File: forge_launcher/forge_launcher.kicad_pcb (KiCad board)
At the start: 4 copper layers, 151.1 x 106 mm, 201 parts, among them J10 Screw_Terminal_01x02, J11 Screw_Terminal_01x02, J12 Screw_Terminal_01x02, J3 Conn_01x06, J7 Screw_Terminal_01x02, J9 Screw_Terminal_01x02, Q1 STR2P3LLH6(Pfet), Q10 MMBT3904, Q2 2N3904, Q3 MMBT3904, Q4 IPD60R145, Q6 IPD60R145, Q9 MMBT3904, SW10 LAUNCH, SW3 ARM, U1 LT3420, U10 AMC3330, U14 AMC3302, U17 AD7352, U18 IR2127, U2 TLV74318, U23 TLV74325, U3 AD7352, U4 TLV74325, U5 LMO78_03-1.0, U6 4945, U8 AMC3330

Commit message: handheld controller PCB layout. Caps, Coil and 4xAA battery holder on bottom side. 2 buttons, 2 leds on topside. ForgeFPGA can mount below with battery removed and 02x13 header sockets added. Will 3d print minimum volume case with buttons and lite pipes.
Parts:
- removed the BT1 at (116.3, 80.8)
- removed the BT1 at (157.5, 80.6)
- removed the H13 at (90.2, 95.2)
- removed the H15 at (91.4, 109.2)
- removed J12: Screw_Terminal_01x02, TerminalBlock_Phoenix:TerminalBlock_Phoenix_MKDS-1,5-2-5.08_1x02_P5.08mm_Horizontal
- removed the PS1 at (236.1, 97.7)
- removed REF** (x2): PinSocket_2x13_P2.54mm_Vertical, Connector_PinSocket_2.54mm:PinSocket_2x13_P2.54mm_Vertical
- removed REF**: SC-82AA, Package_TO_SOT_SMD:SC-82AA
- removed the U5 at (247.1, 96.9)
- removed the U6 at (241.6, 96.9)
- added BT1: ~, myspace pcb:BAT_BH4AA-PC, B.Cu at (233.9, 115.1)
- added C24: 100u 400V, myspace pcb:CAP_radial_18mmdia_38mmh, B.Cu at (213.2, 33.8)
- added C25: 100u 400V, myspace pcb:CAP_radial_18mmdia_38mmh_L, B.Cu at (261.5, 33.8)
- added L1: 390uH 5A, Inductor_THT:L_Toroid_Horizontal_D32.5mm_P28.90mm_Bourns_2300, B.Cu at (234.9, 70.8)
- C17: value CP_Radial_Tantal_D8.0mm_P2.50mm -> 100u 20v
- C18, D1, Q10, Q3, Q9, R108, R11, R15, R31, R32, R4, U2, U23, U4: moved to F.Cu
- J1, J2: renamed from REF**; value PinSocket_2x13_P2.54mm_Vertical -> Conn_02x13_Odd_Even
- J7: moved to B.Cu
- U5: renamed from REF**; value Converter_DCDC_Murata_OKI-78SR_Horizontal -> LMO78_03-1.0
- U6: renamed from REF**; value Converter_DCDC_Murata_OKI-78SR_Horizontal -> 4945
- moved H4 202.9 mm to (264.8, 109.9)
- moved H11 195.1 mm to (234.3, 142.2)
- moved H8 193.5 mm to (245.7, 106.7)
- moved H10 187.8 mm to (259.7, 45.1)
- moved H14 160.2 mm to (264.8, 29.8)
- moved C15 155.6 mm to (259.1, 74.9)
- moved U1 153.9 mm to (264.2, 91.4), turned to 0 degrees
- moved TR1 150.0 mm to (260.4, 82.5), turned to 45 degrees
- moved D5 149.0 mm to (259.4, 71.5), turned to 90 degrees
- moved Q6 146.5 mm to (245.7, 67.3), turned to 90 degrees
- moved R3 143.8 mm to (244.5, 49.5), turned to 90 degrees
- moved C16 142.6 mm to (258.4, 92.1), turned to 90 degrees
- moved C19 140.2 mm to (255.3, 91.4), turned to 90 degrees
- moved H12 136.5 mm to (207.0, 44.5)
- moved H13 133.4 mm to (224.2, 106.0)
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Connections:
- C17 pad 1: (no net) -> Net-(D3-A)
- C17 pad 2: (no net) -> GND
- J1 pad 1: (no net) -> unconnected-(J1-Pin_1-Pad1)
- J1 pad 10: (no net) -> GND
- J1 pad 11: (no net) -> unconnected-(J1-Pin_11-Pad11)
- J1 pad 12: (no net) -> GND
- J1 pad 13: (no net) -> unconnected-(J1-Pin_13-Pad13)
- J1 pad 14: (no net) -> GND
- J1 pad 15: (no net) -> unconnected-(J1-Pin_15-Pad15)
- J1 pad 16: (no net) -> GND
- J1 pad 17: (no net) -> unconnected-(J1-Pin_17-Pad17)
- J1 pad 18: (no net) -> GND
- J1 pad 19: (no net) -> unconnected-(J1-Pin_19-Pad19)
- J1 pad 2: (no net) -> GND
- J1 pad 20: (no net) -> GND
- J1 pad 21: (no net) -> unconnected-(J1-Pin_21-Pad21)
- J1 pad 22: (no net) -> GND
- J1 pad 23: (no net) -> unconnected-(J1-Pin_23-Pad23)
- J1 pad 24: (no net) -> GND
- J1 pad 25: (no net) -> unconnected-(J1-Pin_25-Pad25)
- J1 pad 26: (no net) -> GND
- J1 pad 3: (no net) -> unconnected-(J1-Pin_3-Pad3)
- J1 pad 4: (no net) -> GND
- J1 pad 5: (no net) -> unconnected-(J1-Pin_5-Pad5)
- J1 pad 6: (no net) -> GND
- J1 pad 7: (no net) -> unconnected-(J1-Pin_7-Pad7)
- J1 pad 8: (no net) -> GND
- J1 pad 9: (no net) -> unconnected-(J1-Pin_9-Pad9)
- J2 pad 1: (no net) -> GND
- J2 pad 10: (no net) -> unconnected-(J2-Pin_10-Pad10)
- J2 pad 11: (no net) -> GND
- J2 pad 12: (no net) -> unconnected-(J2-Pin_12-Pad12)
- J2 pad 13: (no net) -> GND
- J2 pad 14: (no net) -> unconnected-(J2-Pin_14-Pad14)
- J2 pad 15: (no net) -> GND
- J2 pad 16: (no net) -> unconnected-(J2-Pin_16-Pad16)
- J2 pad 17: (no net) -> GND
- J2 pad 18: (no net) -> unconnected-(J2-Pin_18-Pad18)
- J2 pad 19: (no net) -> GND
- J2 pad 2: (no net) -> unconnected-(J2-Pin_2-Pad2)
- J2 pad 20: (no net) -> unconnected-(J2-Pin_20-Pad20)
- J2 pad 21: (no net) -> GND
- J2 pad 22: (no net) -> unconnected-(J2-Pin_22-Pad22)
- J2 pad 23: (no net) -> GND
- J2 pad 24: (no net) -> unconnected-(J2-Pin_24-Pad24)
- J2 pad 25: (no net) -> GND
- J2 pad 26: (no net) -> unconnected-(J2-Pin_26-Pad26)
- J2 pad 3: (no net) -> GND
- J2 pad 4: (no net) -> unconnected-(J2-Pin_4-Pad4)
- J2 pad 5: (no net) -> GND
- J2 pad 6: (no net) -> unconnected-(J2-Pin_6-Pad6)
- J2 pad 7: (no net) -> GND
- J2 pad 8: (no net) -> unconnected-(J2-Pin_8-Pad8)
- J2 pad 9: (no net) -> GND
- U19 pad 25: (no net) -> GND
- U5 pad 1: (no net) -> +12V
- U5 pad 2: (no net) -> GND
- U5 pad 3: (no net) -> +3.3V
- U6 pad 1: (no net) -> +BATT
- U6 pad 2: (no net) -> GND
- U6 pad 3: (no net) -> +12V
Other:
- board size 151.1 x 106 mm -> 68 x 118 mm
- board text added: "CASE"
- board text added: "CHARGE"
- board text added: "CONT"
- board text removed: "B"

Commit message: Landscape style PCB initial layout 3d. Large components on bottom as per model. Forge emulator connector section of PCB can be cut away, but also has a spare fpga land point.
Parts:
- removed J10, J11, J7: Screw_Terminal_01x02, TerminalBlock_Phoenix:TerminalBlock_Phoenix_MKDS-1,5-2-5.08_1x02_P5.08mm_Horizontal
- added BT2: BatteryHolder_Keystone_2462_2xAA, Battery:BatteryHolder_Keystone_2462_2xAA, B.Cu at (115.5, 104.2)
- added D6: ES1J, Diode_SMD:D_SMA, F.Cu at (168.3, 64.1)
- added D7: ES1J, Diode_SMD:D_SMA, F.Cu at (168.3, 67.9)
- added R12: 10K, Resistor_SMD:R_0603_1608Metric, B.Cu at (184.2, 78.1)
- added REF**: CalTest_CT3151, Connector:CalTest_CT3151, B.Cu at (153.5, 42.3)
- added REF**: CalTest_CT3151, Connector:CalTest_CT3151, B.Cu at (131.0, 42.3)
- added U19: ~, Package_DFN_QFN:QFN-24-1EP_3x3mm_P0.4mm_EP1.75x1.6mm_ThermalVias, F.Cu at (144.5, 131.5)
- added U2: TLV74318, Package_TO_SOT_SMD:SOT-23-5, B.Cu at (134.5, 132.0)
- BT1: footprint myspace pcb:BAT_BH4AA-PC -> Battery:BatteryHolder_Keystone_2462_2xAA
- C16, C18, C19, D1, D3, PS1, Q1, Q10, Q2, Q3, Q9, R1, R10, R108, R11, R110, R13, R15, R2, R29, R31, R32, R4, R5, R8, U2, U23, U4: moved to B.Cu
- C17: footprint Capacitor_THT:CP_Radial_Tantal_D8.0mm_P2.50mm -> Capacitor_THT:CP_Radial_D8.0mm_P5.00mm; moved to B.Cu
- J9: footprint TerminalBlock_Phoenix:TerminalBlock_Phoenix_MKDS-1,5-2-5.08_1x02_P5.08mm_Horizontal -> Connector_BarrelJack:BarrelJack_CUI_PJ-102AH_Horizontal
- L1: footprint Inductor_THT:L_Toroid_Horizontal_D32.5mm_P28.90mm_Bourns_2300 -> Inductor_THT:L_Toroid_Vertical_L31.8mm_W15.9mm_P13.50mm_Bourns_5700
- moved H4 184.0 mm to (93.3, 43.2)
- moved H12 155.3 mm to (93.5, 150.5)
- moved H5 136.8 mm to (93.5, 111.5)
- moved TP1 135.7 mm to (20.9, 99.4)
- moved TP2 135.7 mm to (20.9, 103.7)
- moved TP3 135.7 mm to (25.2, 99.4)
- moved TP4 135.7 mm to (25.2, 103.7)
- moved TP5 135.7 mm to (29.6, 99.4)
- moved TP6 135.7 mm to (29.6, 103.7)
- moved H11 133.5 mm to (144.8, 43.2)
- moved J9 129.9 mm to (104.8, 84.5), turned to -90 degrees
- moved R20 126.2 mm to (36.7, 88.4)
- moved R21 126.2 mm to (36.7, 90.9)
- moved R22 126.2 mm to (36.7, 93.5)
- moved R24 126.2 mm to (36.7, 96.0)
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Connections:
- C14 pad 1: +1V8 -> +1V1
- C17 pad 1: Net-(D3-A) -> Net-(D6-K)
- Q1 pad 1: Net-(Q1-G) -> Net-(D7-K)
- Q1 pad 2: Net-(D3-A) -> Net-(D6-K)
- Q2 pad 3: Net-(Q1-G) -> Net-(D7-A)
- R1 pad 2: Net-(Q1-G) -> Net-(D7-K)
- U19 pad 22: +1V2 -> +1V1
- U2 pad 5: +1V8 -> +1V1
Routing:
- net GND: track 19.9 -> 0.00 mm, vias 1 -> 0
- net /DisG: track 1.19 -> 0.00 mm
- net (no net): vias 0 -> 48
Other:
- board size 68 x 118 mm -> 109 x 115 mm
- board text added: "ForgeFPGA Eval Board Connector"
- board text added: "spare"
- board text removed: "1"
- board text removed: "2"
- board text removed: "CASE"

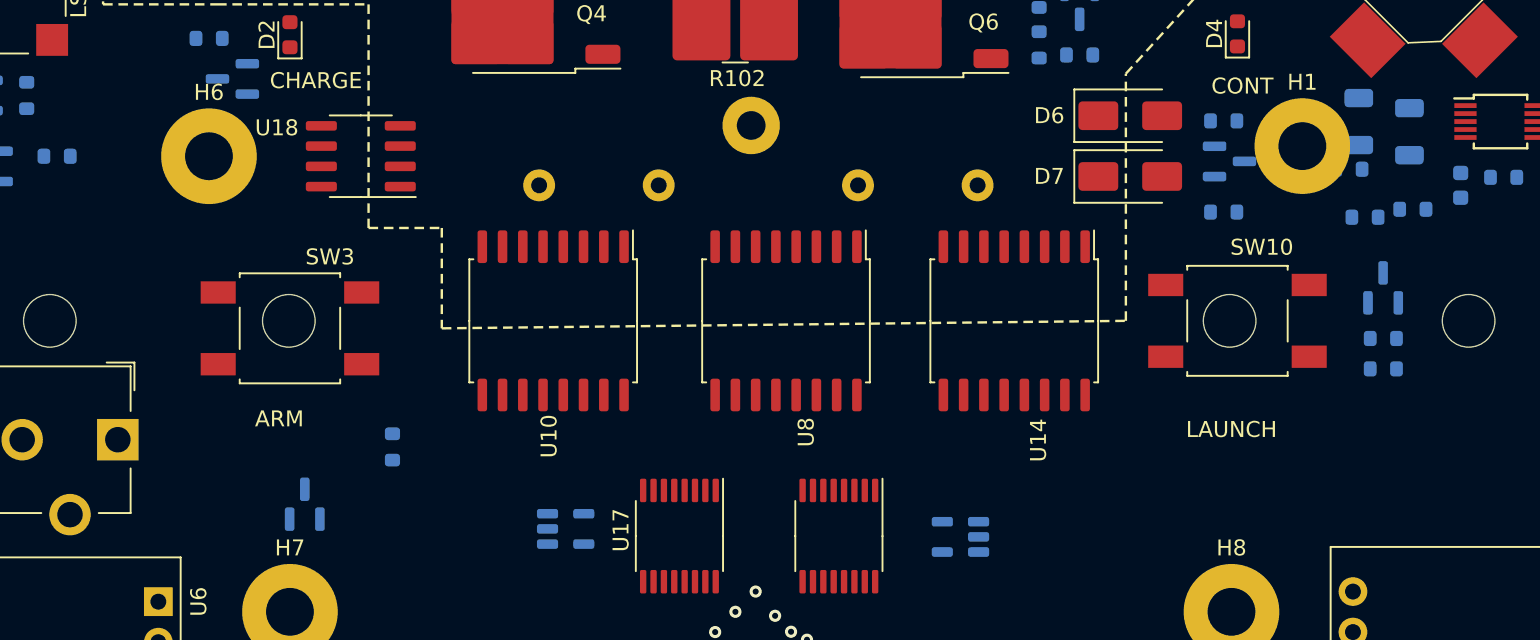
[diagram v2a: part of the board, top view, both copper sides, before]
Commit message: Added component for 3d button frogs (better name than push-button-with-spring-for-tactile-switch)
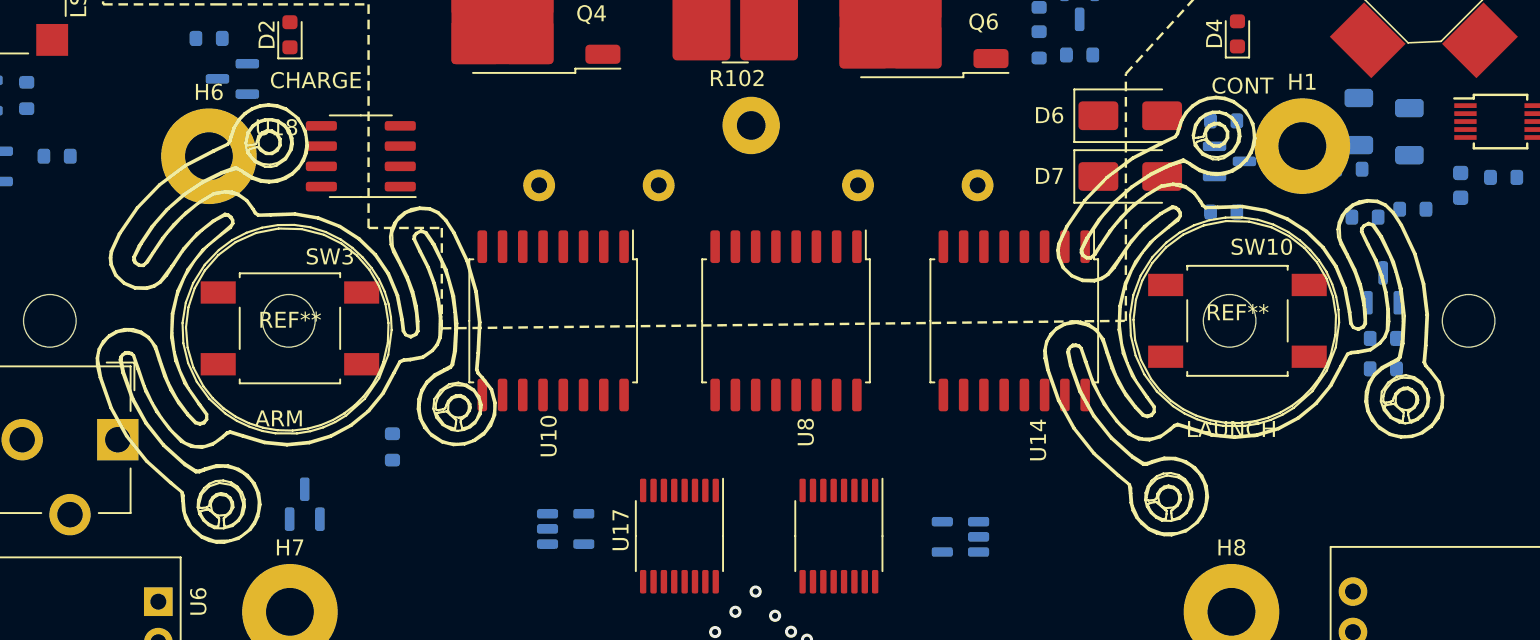
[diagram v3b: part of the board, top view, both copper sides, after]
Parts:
- added REF**: button_frog, myspace pcb:button_frog, F.Cu at (115.6, 77.5)
- added REF**: button_frog, myspace pcb:button_frog, F.Cu at (175.0, 77.0)

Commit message: Update to last ver before fork
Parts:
- removed D3: BAV99, Package_TO_SOT_SMD:SOT-23
- removed FB2: Ferrite, Inductor_SMD:L_0603_1608Metric
- removed the H1 at (179.1, 66.0)
- removed H10, H11, H12, H14, H15, H5, H6, H7, H8: ~, MountingHole:MountingHole_3mm_Pad
- removed J3: Conn_01x06, Connector_PinHeader_2.54mm:PinHeader_1x06_P2.54mm_Vertical
- removed R86: 22R, Resistor_SMD:R_0603_1608Metric
- added C27: 0.1u, Capacitor_SMD:C_0603_1608Metric, B.Cu at (180.1, 65.3)
- added C28: 1u, Capacitor_SMD:C_0603_1608Metric, B.Cu at (161.8, 99.6)
- added C29: 2.2n, Capacitor_SMD:C_0603_1608Metric, B.Cu at (148.6, 86.9)
- added C30: 2.2n, Capacitor_SMD:C_0603_1608Metric, B.Cu at (148.3, 84.8)
- added C31: 0.01u, Capacitor_SMD:C_0603_1608Metric, B.Cu at (145.8, 90.7)
- added C32: 1u, Capacitor_SMD:C_0603_1608Metric, B.Cu at (155.0, 100.6)
- added C35: 4.7u, Capacitor_SMD:C_1206_3216Metric, F.Cu at (160.3, 132.5)
- added C36: 4.7u, Capacitor_SMD:C_1206_3216Metric, F.Cu at (161.8, 100.8)
- added C40: 1u, Capacitor_SMD:C_0603_1608Metric, B.Cu at (190.0, 69.3)
- added GD1: GDT 500V, myspace pcb:GDT_SM1812, F.Cu at (147.2, 58.3)
- added J5: Conn_01x06, Connector_PinHeader_2.54mm:PinHeader_2x03_P2.54mm_Vertical_SMD, F.Cu at (125.0, 101.6)
- added Q5: IRLML0060TRPBF, Package_TO_SOT_SMD:SOT-23, F.Cu at (182.9, 65.3)
- added R14: 10K, Resistor_SMD:R_0603_1608Metric, B.Cu at (186.4, 69.3)
- added R23: 22R, Resistor_SMD:R_0603_1608Metric, B.Cu at (186.4, 70.9)
- added R25: 10.01K, Resistor_SMD:R_0603_1608Metric, B.Cu at (142.5, 89.2)
- added R26: 0, Resistor_SMD:R_0603_1608Metric, B.Cu at (145.8, 92.2)
- added R27: 1.001K, Resistor_SMD:R_0603_1608Metric, B.Cu at (145.8, 89.2)
- added R35: 51R, Resistor_SMD:R_0603_1608Metric, B.Cu at (144.8, 86.9)
- added R36: 51R, Resistor_SMD:R_0603_1608Metric, B.Cu at (146.3, 86.9)
- added R37: np, Resistor_SMD:R_0603_1608Metric, B.Cu at (123.4, 88.3)
- added R38: np, Resistor_SMD:R_0603_1608Metric, B.Cu at (122.2, 88.3)
- added R41: np, Resistor_SMD:R_0603_1608Metric, B.Cu at (122.2, 91.6)
- added R42: np, Resistor_SMD:R_0603_1608Metric, B.Cu at (123.4, 91.6)
- added R43: 10K, Resistor_SMD:R_0603_1608Metric, B.Cu at (161.8, 101.9)
- added R44: 3k3, Resistor_SMD:R_0603_1608Metric, B.Cu at (124.7, 88.3)
- added R45: np, Resistor_SMD:R_0603_1608Metric, B.Cu at (124.6, 91.6)
- added R46: 1K, Resistor_SMD:R_0603_1608Metric, B.Cu at (115.1, 95.2)
- added R47: 22R, Resistor_SMD:R_0603_1608Metric, B.Cu at (115.1, 98.8)
- added R48: 22R, Resistor_SMD:R_0603_1608Metric, B.Cu at (116.2, 90.7)
- added R50: 22R, Resistor_SMD:R_0603_1608Metric, B.Cu at (169.9, 76.6)
- added R53: 10K, Resistor_SMD:R_0603_1608Metric, B.Cu at (100.3, 81.2)
- added R54: 22R, Resistor_SMD:R_0603_1608Metric, B.Cu at (100.3, 83.4)
- added R55: 0, Resistor_SMD:R_0603_1608Metric, B.Cu at (187.2, 59.4)
- added SW1: SW_SPST, Button_Switch_THT:SW_E-Switch_EG1224_SPDT_Angled, F.Cu at (96.8, 76.7)
- added U11: AT25xxx, Package_SO:SOIC-8_3.9x4.9mm_P1.27mm, F.Cu at (122.7, 90.9)
- added U13: LM809, Package_TO_SOT_SMD:SOT-23, B.Cu at (113.8, 90.7)
- added U7: MCP1416, Package_TO_SOT_SMD:SOT-23-5, B.Cu at (183.4, 65.3)
- added X1: ASE-48MHz, Oscillator:Oscillator_SMD_Abracon_ASV-4Pin_7.0x5.1mm_HandSoldering, F.Cu at (115.1, 97.0)
- BT2: value BatteryHolder_Keystone_2462_2xAA -> ~
- C1, C10, C11, C128, C129, C13, C14, C2, C20, C22, C23, C26, C3, C33, C34, C37, C38, C39, C4, C44, C45, C46, C47, C48, C49, C5, C50, C53, C54, C55, C56, C57, C6, C60, C62, C64, C65, C66, C69, C7, C70, C71, C73, C74, C75, C76, C77, C78, C79, C80, C81, C82, C83, C84, C9, FB5, FB6, FB7, R103, R104, R105, R16, R17, R18, R19, R20, R21, R22, R24, R28, R30, R33, R34, R39, R40, R49, R51, R52, R6, R61, R62, R63, R64, R67, R68, R69, R7, R70, R79, R80, R81, R82, R83, R9, R98, R99: moved to B.Cu
- C16: value 4.7u -> 1u; footprint Capacitor_SMD:C_1206_3216Metric -> Capacitor_SMD:C_0603_1608Metric
- C17: footprint Capacitor_THT:CP_Radial_D8.0mm_P5.00mm -> Capacitor_THT:C_Radial_D5.0mm_H7.0mm_P2.00mm
- C18: value 1u -> 4.7u; footprint Capacitor_SMD:C_0603_1608Metric -> Capacitor_SMD:C_1206_3216Metric; moved to F.Cu
- C19: moved to F.Cu
- FR1, FR2: renamed from REF**; value button_frog -> ~
- J4, J7: renamed from REF**; value CalTest_CT3151 -> Jack; footprint Connector:CalTest_CT3151 -> myspace pcb:CalTest_CT3151
- J9: value Screw_Terminal_01x02 -> Barrel_Jack; footprint Connector_BarrelJack:BarrelJack_CUI_PJ-102AH_Horizontal -> Connector_BarrelJack:BarrelJack_CUI_PJ-063AH_Horizontal
- L1: footprint Inductor_THT:L_Toroid_Vertical_L31.8mm_W15.9mm_P13.50mm_Bourns_5700 -> Inductor_THT:L_Toroid_Vertical_L35.6mm_W17.8mm_P12.70mm_Pulse_E
- PS1: footprint Converter_DCDC:Converter_DCDC_Murata_MEE1SxxxxSC_THT -> myspace pcb:RM-1212
- R13: value 10K -> 51.1K
- R29: value 51.1K -> 100K
- R32: value 100K -> np
- R5: value 10K -> 10R
- TR1: footprint myspace pcb:PA0637A Pulse Coil -> myspace pcb:PA0637A Pulse Coil 3D
- U19: footprint Package_DFN_QFN:QFN-24-1EP_3x3mm_P0.4mm_EP1.75x1.6mm_ThermalVias -> myspace pcb:QFN-24-3x3mm
- U9: renamed from U19; footprint Package_DFN_QFN:QFN-24-1EP_3x3mm_P0.4mm_EP1.75x1.6mm_ThermalVias -> myspace pcb:QFN-24-3x3mm
- moved TP4 178.3 mm to (197.4, 57.1)
- moved TP3 170.3 mm to (194.8, 83.6)
- moved C34 163.8 mm to (186.2, 98.0), turned to 90 degrees
- moved C33 163.6 mm to (186.2, 94.5), turned to -90 degrees
- moved C65 156.4 mm to (184.4, 98.0), turned to 90 degrees
- moved C66 155.9 mm to (184.4, 94.5), turned to -90 degrees
- moved C7 148.1 mm to (159.0, 131.2), turned to 180 degrees
- moved C14 137.8 mm to (152.1, 132.3), turned to -90 degrees
- moved R7 136.2 mm to (159.0, 133.3), turned to 180 degrees
- moved C22 136.1 mm to (156.7, 92.2)
- moved TP5 132.9 mm to (162.3, 105.7)
- moved C69 131.9 mm to (160.5, 83.6), turned to 180 degrees
- moved C71 129.8 mm to (158.0, 81.5)
- moved C9 129.7 mm to (150.1, 89.2)
- moved C78 129.1 mm to (161.8, 72.9), turned to 90 degrees
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- renumbered H4 to H1, H13 to H4, U2 to U12
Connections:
- BT1 pad 2: GND -> /BINT
- BT2 pad 1: (no net) -> /BINT
- BT2 pad 2: (no net) -> GND
- C18 pad 1: Net-(U1-CT) -> +3.3V
- C38 pad 1: /vina0+ -> /vina1+
- C39 pad 1: /vina0- -> /vina1-
- C53 pad 2: Net-(U14-DCDC_GND) -> GND
- C54 pad 1: /vina1+ -> /vinb1+
- C55 pad 1: /vinb1+ -> /vina0+
- C56 pad 1: /vina1- -> /vinb1-
- C57 pad 1: /vinb1- -> /vina0-
- C69 pad 2: Net-(U8-DCDC_GND) -> GND
- C82 pad 2: Net-(U10-DCDC_GND) -> GND
- H2 pad 1: unconnected-(H2-Pad1) -> GND
- H3 pad 1: unconnected-(H3-Pad1) -> GND
- H4 pad 1: unconnected-(H13-Pad1) -> GND
- H9 pad 1: unconnected-(H9-Pad1) -> GND
- J1 pad 1: unconnected-(J1-Pin_1-Pad1) -> GND
- J1 pad 11: unconnected-(J1-Pin_11-Pad11) -> /sclk
- J1 pad 13: unconnected-(J1-Pin_13-Pad13) -> /dataA0
- J1 pad 15: unconnected-(J1-Pin_15-Pad15) -> /dataB0
- J1 pad 17: unconnected-(J1-Pin_17-Pad17) -> /dataA1
- J1 pad 19: unconnected-(J1-Pin_19-Pad19) -> /dataB1
- J1 pad 21: unconnected-(J1-Pin_21-Pad21) -> /cs
- J1 pad 23: unconnected-(J1-Pin_23-Pad23) -> /pwm
- J1 pad 25: unconnected-(J1-Pin_25-Pad25) -> /arm_led
- J1 pad 3: unconnected-(J1-Pin_3-Pad3) -> +1V1
- J1 pad 5: unconnected-(J1-Pin_5-Pad5) -> /cont_led
- J1 pad 7: unconnected-(J1-Pin_7-Pad7) -> /launch_n
- J1 pad 9: unconnected-(J1-Pin_9-Pad9) -> /dump
- J2 pad 10: unconnected-(J2-Pin_10-Pad10) -> /spi_si
- J2 pad 12: unconnected-(J2-Pin_12-Pad12) -> /spi_ss
- J2 pad 14: unconnected-(J2-Pin_14-Pad14) -> /spi_ck
- J2 pad 16: unconnected-(J2-Pin_16-Pad16) -> /osc
- J2 pad 18: unconnected-(J2-Pin_18-Pad18) -> /mute_n
- J2 pad 2: unconnected-(J2-Pin_2-Pad2) -> GND
- J2 pad 20: unconnected-(J2-Pin_20-Pad20) -> /speaker
- J2 pad 22: unconnected-(J2-Pin_22-Pad22) -> GND
- J2 pad 24: unconnected-(J2-Pin_24-Pad24) -> /reset_n
- J2 pad 26: unconnected-(J2-Pin_26-Pad26) -> /sleep_n
- J2 pad 4: unconnected-(J2-Pin_4-Pad4) -> +3.3V
- J2 pad 6: unconnected-(J2-Pin_6-Pad6) -> /charge
- J2 pad 8: unconnected-(J2-Pin_8-Pad8) -> /spi_so
- J4 pad 1: (no net) -> /+OUT
- J7 pad 1: (no net) -> GND
- J9 pad 1: GND -> /B+
- J9 pad 2: +BATT -> GND
- R13 pad 1: GND -> Net-(U1-RFB)
- R13 pad 2: /charge -> /SW
- R29 pad 1: Net-(U1-RFB) -> /done
- R29 pad 2: /SW -> +3.3V
- R32 pad 1: /done -> GND
- R32 pad 2: +3.3V -> Net-(R32-Pad2)
- R39 pad 2: /vina0+ -> /vina1+
- R40 pad 2: /vina0- -> /vina1-
- R5 pad 2: +12V -> Net-(Q5-G)
- R61 pad 2: /vina1+ -> /vinb1+
- R62 pad 2: /vina1- -> /vinb1-
- R63 pad 2: /vinb1+ -> /vina0+
- R64 pad 2: /vinb1- -> /vina0-
- R83 pad 1: Net-(R83-Pad1) -> +3.3V
- R83 pad 2: GND -> Net-(R50-Pad2)
- R9 pad 2: /pwm -> /pwmr
- SW10 pad 1: Net-(R83-Pad1) -> GND
- SW10 pad 2: +3.3V -> Net-(R50-Pad2)
- TR1 pad 1: Net-(U1-SEC) -> Net-(R32-Pad2)
- U1 pad 9: /charge -> Net-(U1-CHRG)
- U10 pad 15: Net-(U10-DCDC_GND) -> GND
- U12 pad 3: Net-(U2-EN) -> Net-(U12-EN)
- U12 pad 4: unconnected-(U2-NC-Pad4) -> unconnected-(U12-NC-Pad4)
- U14 pad 15: Net-(U14-DCDC_GND) -> GND
- U19 pad 1: /cs -> /dump
- U19 pad 10: unconnected-(U19-nSLEEP-Pad10) -> /sleep_n
- U19 pad 13: /dataA0 -> /speaker
- U19 pad 14: /sclk -> /mute_n
- U19 pad 16: unconnected-(U19-GPIO3/SPI_CK-Pad16) -> /spi_ck
- U19 pad 17: unconnected-(U19-GPIO4/SPI_SS-Pad17) -> /spi_ss
- U19 pad 18: unconnected-(U19-GPIO5/SPI_SI-Pad18) -> /spi_si
- U19 pad 19: unconnected-(U19-GPIO6/SPI_SO-Pad19) -> /spi_so
- U19 pad 2: /dump -> /sclk
- U19 pad 20: /dataB0 -> /charge
- U19 pad 23: /dataA1 -> /cont_led
- U19 pad 24: /dataB1 -> /launch_n
- U19 pad 3: /charge -> /dataA0
- U19 pad 4: /done -> /dataB0
- U19 pad 5: /pwm -> /dataA1
- U19 pad 6: /arm_led -> /dataB1
- U19 pad 7: /cont_led -> /cs
- U19 pad 8: /speaker -> /pwm
- U19 pad 9: /launch -> /arm_led
- U8 pad 15: Net-(U8-DCDC_GND) -> GND
- U9 pad 1: /cs -> /dump
- U9 pad 10: unconnected-(U19-nSLEEP-Pad10) -> /sleep_n
- U9 pad 13: /dataA0 -> /speaker
- U9 pad 14: /sclk -> /mute_n
- U9 pad 16: unconnected-(U19-GPIO3/SPI_CK-Pad16) -> /spi_ck
- U9 pad 17: unconnected-(U19-GPIO4/SPI_SS-Pad17) -> /spi_ss
- U9 pad 18: unconnected-(U19-GPIO5/SPI_SI-Pad18) -> /spi_si
- U9 pad 19: unconnected-(U19-GPIO6/SPI_SO-Pad19) -> /spi_so
- U9 pad 2: /dump -> /sclk
- U9 pad 20: /dataB0 -> /charge
- U9 pad 23: /dataA1 -> /cont_led
- U9 pad 24: /dataB1 -> /launch_n
- U9 pad 3: /charge -> /dataA0
- U9 pad 4: /done -> /dataB0
- U9 pad 5: /pwm -> /dataA1
- U9 pad 6: /arm_led -> /dataB1
- U9 pad 7: /cont_led -> /cs
- U9 pad 8: /speaker -> /pwm
- U9 pad 9: /launch -> /arm_led
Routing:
- net GND: track 0.00 -> 220.2 mm, vias 0 -> 89
- net /speaker: track 0.00 -> 140.6 mm, vias 0 -> 3
- net /arm_led: track 0.00 -> 137.1 mm, vias 0 -> 2
- net +3.3V: track 0.00 -> 131.5 mm, vias 0 -> 33
- net /pwm: track 0.00 -> 128.0 mm, vias 0 -> 2
- net /cont_led: track 0.00 -> 123.9 mm, vias 0 -> 2
- net /charge: track 0.00 -> 118.8 mm, vias 0 -> 3
- net /mute_n: track 0.00 -> 115.7 mm, vias 0 -> 3
- net /spi_so: track 0.00 -> 110.3 mm, vias 0 -> 2
- net /dump: track 0.00 -> 108.7 mm, vias 0 -> 2
- net /reset_n: track 0.00 -> 103.8 mm, vias 0 -> 3
- net /spi_ss: track 0.00 -> 103.1 mm, vias 0 -> 3
- net /launch_n: track 0.00 -> 99.8 mm, vias 0 -> 2
- net /spi_si: track 0.00 -> 97.6 mm, vias 0 -> 2
- net /osc: track 0.00 -> 87.8 mm, vias 0 -> 3
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- added copper zone on In4.Cu, net +12V
- added copper zone on In3.Cu, net +1V1
- added copper zone on In2.Cu, net +3.3V
- added copper zone on In4.Cu, net +3.3V
- added copper zone on F.Cu, net +300V
- added copper zone on F.Cu, net +BATT
- added copper zone on In3.Cu, net +BATT
- added copper zone on F.Cu, net +VSW
- added copper zone on F.Cu, net /+OUT
- added copper zone on F.Cu, net /B+
- added copper zone on In3.Cu, net /B+
- added copper zone on In3.Cu, net /BINT
- added copper zone on In3.Cu, net /HGNDCV
- added copper zone on In3.Cu, net /HGNDLI
- added copper zone on In3.Cu, net /HGNDLV
- added copper zone on F.Cu, net /LSEN
- added copper zone on F.Cu, net /SW
- added copper zone on F.Cu, net /SWDIS
- added copper zone on F.Cu, net GND
- added copper zone on In1.Cu, net GND
- added copper zone on In2.Cu, net GND
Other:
- outline, holes or cut-outs redrawn
- copper layers 4 -> 6
- board text added: "+"
- board text added: "Alt"
- board text added: "CHARGE LED"
- board text added: "CONT LED"
- board text added: "Eval Connector"
- board text added: "LAUNCH"
- board text added: "SPI"
- board text added: "XS"
- board text removed: "CHARGE"
- board text removed: "CONT"
- board text removed: "ForgeFPGA Eval Board Connector"
- board text removed: "Launch Control FPGA"
- board text removed: "spare"
